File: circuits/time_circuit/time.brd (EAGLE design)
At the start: 28.9 x 38.1 mm, 8 parts

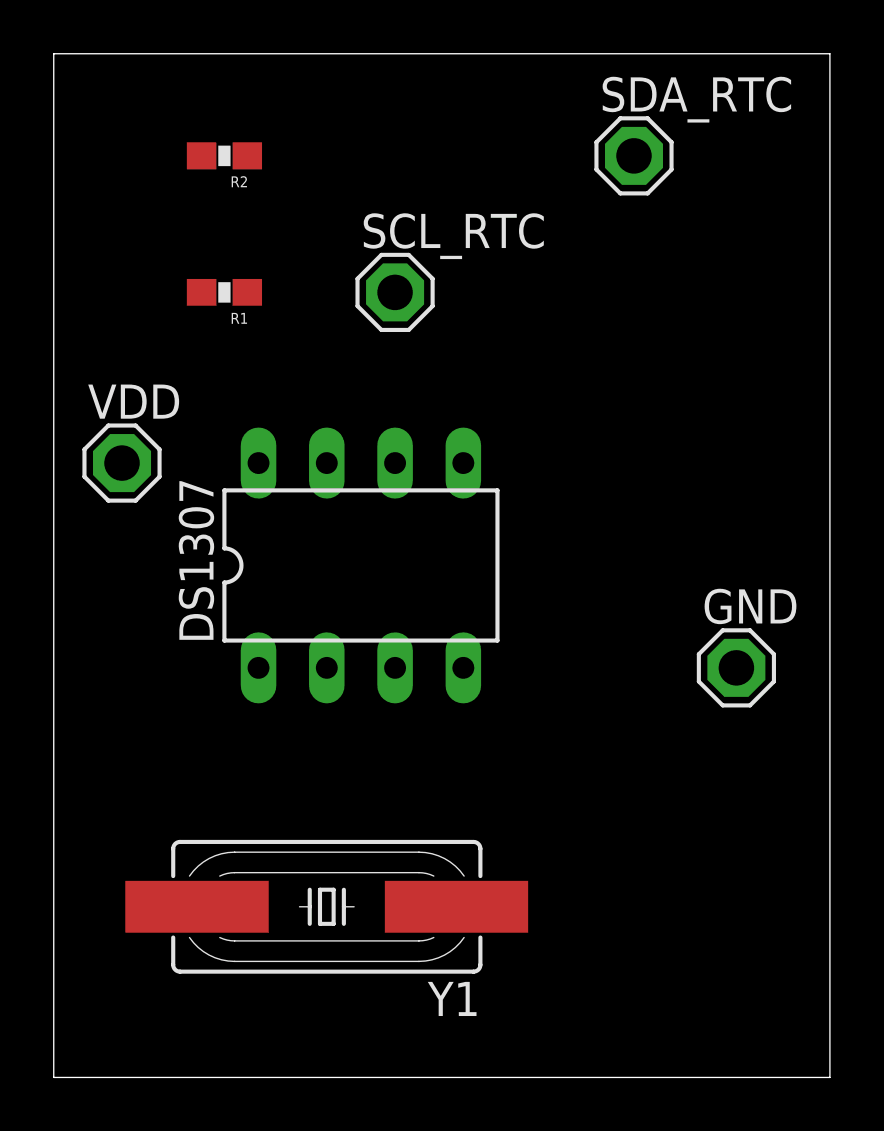
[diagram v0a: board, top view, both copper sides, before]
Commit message: time circuit revised
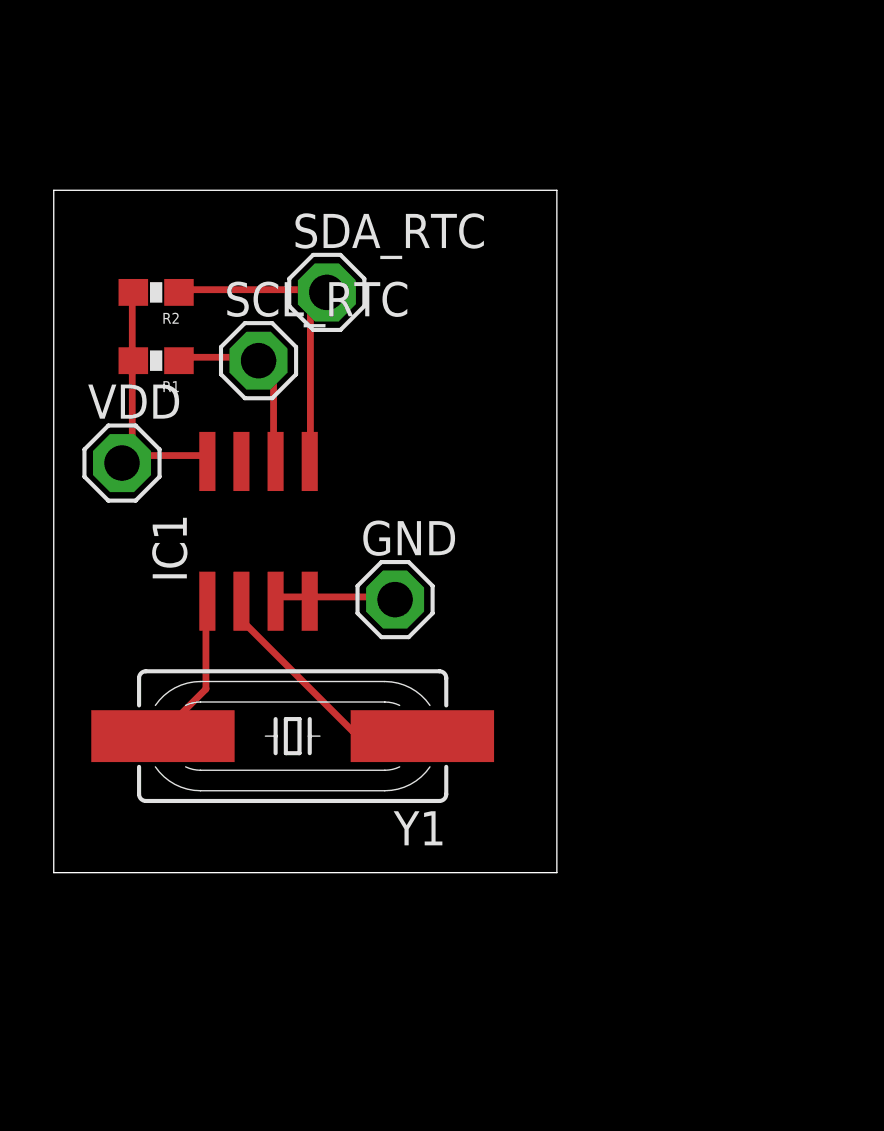
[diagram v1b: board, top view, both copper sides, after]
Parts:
- removed DS1307: DS1307, ds1307_pcf8583:DIL08
- added IC1: DS1307Z, ds1307_pcf8583:SOIC8
- moved GND 13.0 mm to (52.1, 47.0)
- moved SDA_RTC 12.5 mm to (49.5, 58.4)
- moved Y1 6.48 mm to (48.3, 41.9)
- moved R2 5.68 mm to (43.2, 58.4)
- moved SCL_RTC 5.68 mm to (47.0, 55.9)
- moved R1 3.59 mm to (43.2, 55.9)
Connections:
- net GND: now also IC1.3, IC1.4; no longer DS1307.3, DS1307.4
- net N$1: now also IC1.6; no longer DS1307.6
- net N$2: now also IC1.5; no longer DS1307.5
- net N$3: now also IC1.2; no longer DS1307.2
- net N$4: now also IC1.1; no longer DS1307.1
- net VDD: now also IC1.8; no longer DS1307.8
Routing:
- net N$2: track 0.00 -> 12.6 mm
- net VDD: track 0.00 -> 10.0 mm
- net N$3: track 0.00 -> 9.26 mm
- net N$1: track 0.00 -> 7.07 mm
- net N$4: track 0.00 -> 5.70 mm
- net GND: track 0.00 -> 4.74 mm
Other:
- board size 28.9 x 38.1 mm -> 18.7 x 25.4 mm
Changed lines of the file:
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@@
 <board>
 <plain>
-<wire x1="39.37" y1="29.21" x2="68.25" y2="29.21" width="0" layer="20"/>
-<wire x1="68.25" y1="29.21" x2="68.25" y2="67.3" width="0" layer="20"/>
-<wire x1="68.25" y1="67.3" x2="39.37" y2="67.3" width="0" layer="20"/>
-<wire x1="39.37" y1="67.3" x2="39.37" y2="29.21" width="0" layer="20"/>
+<wire x1="39.37" y1="36.83" x2="58.09" y2="36.83" width="0" layer="20"/>
+<wire x1="58.09" y1="36.83" x2="58.09" y2="62.22" width="0" layer="20"/>
+<wire x1="58.09" y1="62.22" x2="39.37" y2="62.22" width="0" layer="20"/>
+<wire x1="39.37" y1="62.22" x2="39.37" y2="36.83" width="0" layer="20"/>
 </plain>
 <attributes>
@@
 </autorouter>
 <elements>
-<element name="DS1307" library="ds1307_pcf8583" package="DIL08" value="DS1307" x="50.8" y="48.26"/>
-<element name="GND" library="solpad" package="SE13" value="SE13" x="64.77" y="44.45"/>
-<element name="R1" library="SparkFun-Resistors" package="0603-RES" value="10K" x="45.72" y="58.42" rot="R180">
-<attribute name="PROD_ID" value="RES-00824" x="45.72" y="58.42" size="1.778" layer="27" rot="R180" display="off"/>
+<element name="GND" library="solpad" package="SE13" value="SE13" x="52.07" y="46.99"/>
+<element name="R1" library="SparkFun-Resistors" package="0603-RES" value="10K" x="43.18" y="55.88" rot="R180">
+<attribute name="PROD_ID" value="RES-00824" x="43.18" y="55.88" size="1.778" layer="27" rot="R180" display="off"/>
 </element>
-<element name="R2" library="SparkFun-Resistors" package="0603-RES" value="10K" x="45.72" y="63.5" rot="R180">
-<attribute name="PROD_ID" value="RES-00824" x="45.72" y="63.5" size="1.778" layer="27" rot="R180" display="off"/>
+<element name="R2" library="SparkFun-Resistors" package="0603-RES" value="10K" x="43.18" y="58.42" rot="R180">
+<attribute name="PROD_ID" value="RES-00824" x="43.18" y="58.42" size="1.778" layer="27" rot="R180" display="off"/>
 </element>
-<element name="SCL_RTC" library="solpad" package="SE13" value="SE13" x="52.07" y="58.42"/>
-<element name="SDA_RTC" library="solpad" package="SE13" value="SE13" x="60.96" y="63.5"/>
+<element name="SCL_RTC" library="solpad" package="SE13" value="SE13" x="46.99" y="55.88"/>
+<element name="SDA_RTC" library="solpad" package="SE13" value="SE13" x="49.53" y="58.42"/>
 <element name="VDD" library="solpad" package="SE13" value="SE13" x="41.91" y="52.07"/>
-<element name="Y1" library="SparkFun-FreqCtrl" package="HC49UP" value="" x="49.53" y="35.56" rot="R180"/>
+<element name="Y1" library="SparkFun-FreqCtrl" package="HC49UP" value="" x="48.26" y="41.91" rot="R180"/>
+<element name="IC1" library="ds1307_pcf8583" package="SOIC8" value="DS1307Z" x="46.99" y="49.53"/>
 </elements>
 <signals>
 <signal name="N$1">
-<contactref element="DS1307" pad="6"/>
 <contactref element="SCL_RTC" pad="MP"/>
 <contactref element="R1" pad="1"/>
-<wire x1="46.57" y1="58.42" x2="52.07" y2="58.42" width="0" layer="19" extent="1-1"/>
-<wire x1="52.07" y1="52.07" x2="52.07" y2="58.42" width="0" layer="19" extent="1-1"/>
+<contactref element="IC1" pad="6"/>
+<wire x1="46.863" y1="56.007" x2="44.1198" y2="56.007" width="0.254" layer="1"/>
+<wire x1="44.1198" y1="56.007" x2="44.03" y2="55.88" width="0.254" layer="1"/>
+<wire x1="46.863" y1="56.007" x2="46.99" y2="55.88" width="0.254" layer="1"/>
+<wire x1="47.5488" y1="55.3212" x2="47.5488" y2="52.3494" width="0.254" layer="1"/>
+<wire x1="46.99" y1="55.88" x2="47.5488" y2="55.3212" width="0.254" layer="1"/>
+<wire x1="47.5488" y1="52.3494" x2="47.625" y2="52.13" width="0.254" layer="1"/>
 </signal>
 <signal name="N$2">
-<contactref element="DS1307" pad="5"/>
 <contactref element="R2" pad="1"/>
 <contactref element="SDA_RTC" pad="MP"/>
-<wire x1="60.96" y1="63.5" x2="54.61" y2="52.07" width="0" layer="19" extent="1-1"/>
-<wire x1="46.57" y1="63.5" x2="60.96" y2="63.5" width="0" layer="19" extent="1-1"/>
+<contactref element="IC1" pad="5"/>
+<wire x1="49.3776" y1="58.5216" x2="48.9204" y2="58.5216" width="0.254" layer="1"/>
+<wire x1="48.9204" y1="58.5216" x2="44.1198" y2="58.5216" width="0.254" layer="1"/>
+<wire x1="44.1198" y1="58.5216" x2="44.03" y2="58.42" width="0.254" layer="1"/>
+<wire x1="49.3776" y1="58.5216" x2="49.53" y2="58.42" width="0.254" layer="1"/>
+<wire x1="48.9204" y1="58.5216" x2="48.9204" y2="52.3494" width="0.254" layer="1"/>
+<wire x1="48.9204" y1="52.3494" x2="48.895" y2="52.13" width="0.254" layer="1"/>
+<wire x1="48.9204" y1="58.5216" x2="49.53" y2="58.42" width="0.254" layer="1"/>
 </signal>
 <signal name="N$3">
-<contactref element="DS1307" pad="2"/>
 <contactref element="Y1" pad="1"/>
-<wire x1="54.356" y1="35.56" x2="49.53" y2="44.45" width="0" layer="19" extent="1-1"/>
+<contactref element="IC1" pad="2"/>
+<wire x1="46.4058" y1="46.1772" x2="46.4058" y2="46.863" width="0.254" layer="1"/>
+<wire x1="50.5206" y1="42.0624" x2="46.4058" y2="46.1772" width="0.254" layer="1"/>
+<wire x1="53.0352" y1="42.0624" x2="50.5206" y2="42.0624" width="0.254" layer="1"/>
+<wire x1="46.4058" y1="46.863" x2="46.355" y2="46.93" width="0.254" layer="1"/>
+<wire x1="53.0352" y1="42.0624" x2="53.086" y2="41.91" width="0.254" layer="1"/>
 </signal>
 <signal name="N$4">
-<contactref element="DS1307" pad="1"/>
 <contactref element="Y1" pad="2"/>
-<wire x1="44.704" y1="35.56" x2="46.99" y2="44.45" width="0" layer="19" extent="1-1"/>
+<contactref element="IC1" pad="1"/>
+<wire x1="45.0342" y1="43.6626" x2="45.0342" y2="46.863" width="0.254" layer="1"/>
+<wire x1="43.434" y1="42.0624" x2="45.0342" y2="43.6626" width="0.254" layer="1"/>
+<wire x1="45.0342" y1="46.863" x2="45.085" y2="46.93" width="0.254" layer="1"/>
+<wire x1="43.434" y1="42.0624" x2="43.434" y2="41.91" width="0.254" layer="1"/>
 </signal>
 <signal name="GND">
-<contactref element="DS1307" pad="4"/>
-<contactref element="DS1307" pad="3"/>
 <contactref element="GND" pad="MP"/>
-<wire x1="54.61" y1="44.45" x2="64.77" y2="44.45" width="0" layer="19" extent="1-1"/>
-<wire x1="52.07" y1="44.45" x2="54.61" y2="44.45" width="0" layer="19" extent="1-1"/>
+<contactref element="IC1" pad="4"/>
+<contactref element="IC1" pad="3"/>
+<wire x1="48.6918" y1="47.0916" x2="47.7774" y2="47.0916" width="0.254" layer="1"/>
+<wire x1="47.7774" y1="47.0916" x2="47.625" y2="46.93" width="0.254" layer="1"/>
+<wire x1="48.6918" y1="47.0916" x2="48.895" y2="46.93" width="0.254" layer="1"/>
+<wire x1="51.8922" y1="47.0916" x2="48.9204" y2="47.0916" width="0.254" layer="1"/>
+<wire x1="48.9204" y1="47.0916" x2="48.895" y2="46.93" width="0.254" layer="1"/>
+<wire x1="51.8922" y1="47.0916" x2="52.07" y2="46.99" width="0.254" layer="1"/>
 </signal>
 <signal name="VDD">
-<contactref element="DS1307" pad="8"/>
 <contactref element="R1" pad="2"/>
 <contactref element="R2" pad="2"/>
 <contactref element="VDD" pad="MP"/>
-<wire x1="44.87" y1="58.42" x2="44.87" y2="63.5" width="0" layer="19" extent="1-1"/>
-<wire x1="46.99" y1="52.07" x2="44.87" y2="58.42" width="0" layer="19" extent="1-1"/>
-<wire x1="41.91" y1="52.07" x2="46.99" y2="52.07" width="0" layer="19" extent="1-1"/>
+<contactref element="IC1" pad="8"/>
+<wire x1="42.291" y1="58.293" x2="42.291" y2="56.007" width="0.254" layer="1"/>
+<wire x1="42.291" y1="56.007" x2="42.33" y2="55.88" width="0.254" layer="1"/>
+<wire x1="42.291" y1="58.293" x2="42.33" y2="58.42" width="0.254" layer="1"/>
+<wire x1="42.291" y1="52.3494" x2="42.291" y2="55.7784" width="0.254" layer="1"/>
+<wire x1="42.0624" y1="52.1208" x2="42.291" y2="52.3494" width="0.254" layer="1"/>
+<wire x1="42.291" y1="55.7784" x2="42.33" y2="55.88" width="0.254" layer="1"/>
+<wire x1="42.0624" y1="52.1208" x2="41.91" y2="52.07" width="0.254" layer="1"/>
+<wire x1="42.291" y1="52.3494" x2="45.0342" y2="52.3494" width="0.254" layer="1"/>
+<wire x1="45.0342" y1="52.3494" x2="45.085" y2="52.13" width="0.254" layer="1"/>
+<wire x1="42.291" y1="52.3494" x2="41.91" y2="52.07" width="0.254" layer="1"/>
 </signal>
 </signals>
